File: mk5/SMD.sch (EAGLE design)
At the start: 12 parts, among them IC2 78L05F

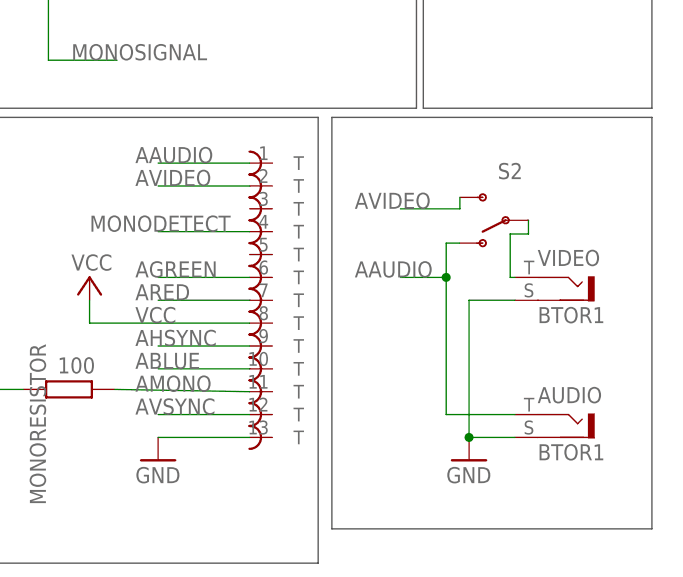
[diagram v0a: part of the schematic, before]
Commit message: Swapped switch pins on A/V switch, to make it easier to patch video to video RCA.
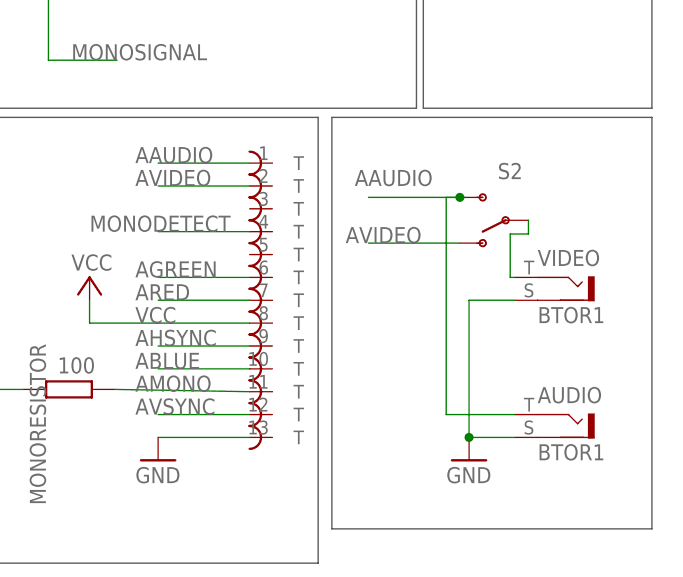
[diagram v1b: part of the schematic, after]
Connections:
- net AAUDIO: now also S2.S; no longer S2.O
- net AVIDEO: now also S2.O; no longer S2.S
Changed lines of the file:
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@@
 <pinref part="AUDIO" gate="G$1" pin="1"/>
 <wire x1="74.676" y1="-6.35" x2="67.056" y2="-6.35" width="0.1524" layer="91"/>
-<wire x1="67.056" y1="-6.35" x2="67.056" y2="8.636" width="0.1524" layer="91"/>
-<wire x1="67.056" y1="8.636" x2="67.056" y2="8.89" width="0.1524" layer="91"/>
-<wire x1="67.056" y1="8.89" x2="61.976" y2="8.89" width="0.1524" layer="91"/>
-<label x="56.896" y="8.89" size="1.778" layer="95"/>
-<wire x1="67.056" y1="8.89" x2="67.056" y2="12.7" width="0.1524" layer="91"/>
-<pinref part="S2" gate="1" pin="O"/>
-<wire x1="67.056" y1="12.7" x2="68.58" y2="12.7" width="0.1524" layer="91"/>
-<junction x="67.056" y="8.89"/>
+<wire x1="67.056" y1="-6.35" x2="67.056" y2="17.78" width="0.1524" layer="91"/>
+<label x="56.896" y="19.05" size="1.778" layer="95"/>
+<pinref part="S2" gate="1" pin="S"/>
+<wire x1="68.58" y1="17.78" x2="67.056" y2="17.78" width="0.1524" layer="91"/>
+<wire x1="68.58" y1="17.78" x2="58.42" y2="17.78" width="0.1524" layer="91"/>
+<junction x="68.58" y="17.78"/>
 </segment>
 <segment>
@@
 <net name="AVIDEO" class="0">
 <segment>
-<wire x1="61.976" y1="16.51" x2="68.58" y2="16.51" width="0.1524" layer="91"/>
-<label x="56.896" y="16.51" size="1.778" layer="95"/>
-<pinref part="S2" gate="1" pin="S"/>
-<wire x1="68.58" y1="17.78" x2="68.58" y2="16.51" width="0.1524" layer="91"/>
-</segment>
-<segment>
 <pinref part="ATARIOUT" gate="G$2" pin="T"/>
 <wire x1="45.212" y1="19.05" x2="35.052" y2="19.05" width="0.1524" layer="91"/>
 <label x="32.512" y="19.05" size="1.778" layer="95"/>
 </segment>
+<segment>
+<pinref part="S2" gate="1" pin="O"/>
+<wire x1="68.58" y1="12.7" x2="58.42" y2="12.7" width="0.1524" layer="91"/>
+<label x="55.88" y="12.7" size="1.778" layer="95"/>
+</segment>
 </net>
